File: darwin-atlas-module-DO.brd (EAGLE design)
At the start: 95 x 25 mm, 24 parts, among them J1 2X6-HEADERS, U3 M24C02-WMN6TP

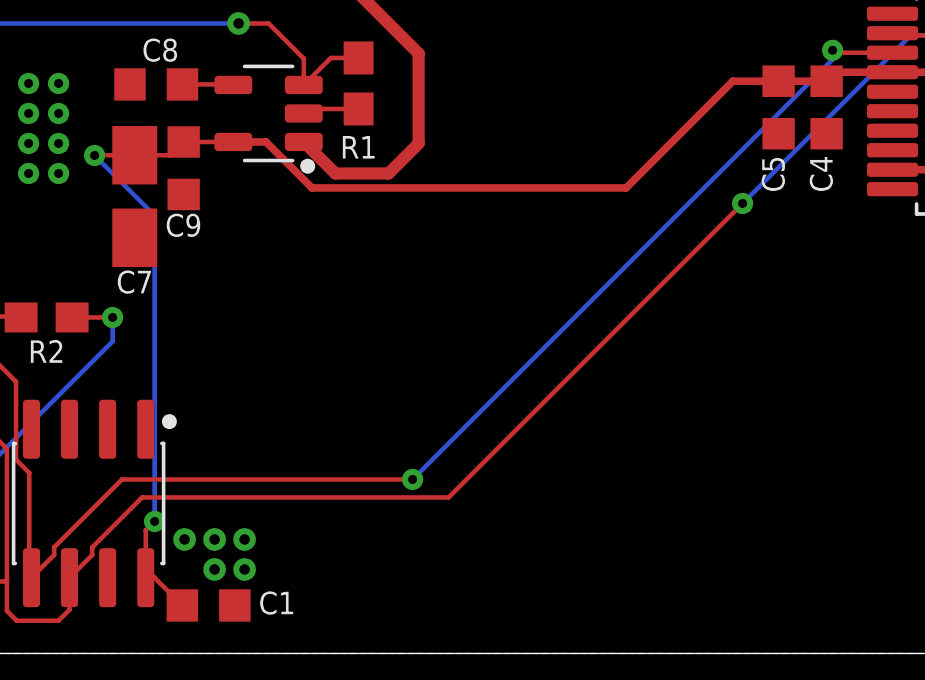
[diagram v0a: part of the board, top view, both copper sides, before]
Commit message: Forked D.O. Variant and added barometric pressure sensor to it.
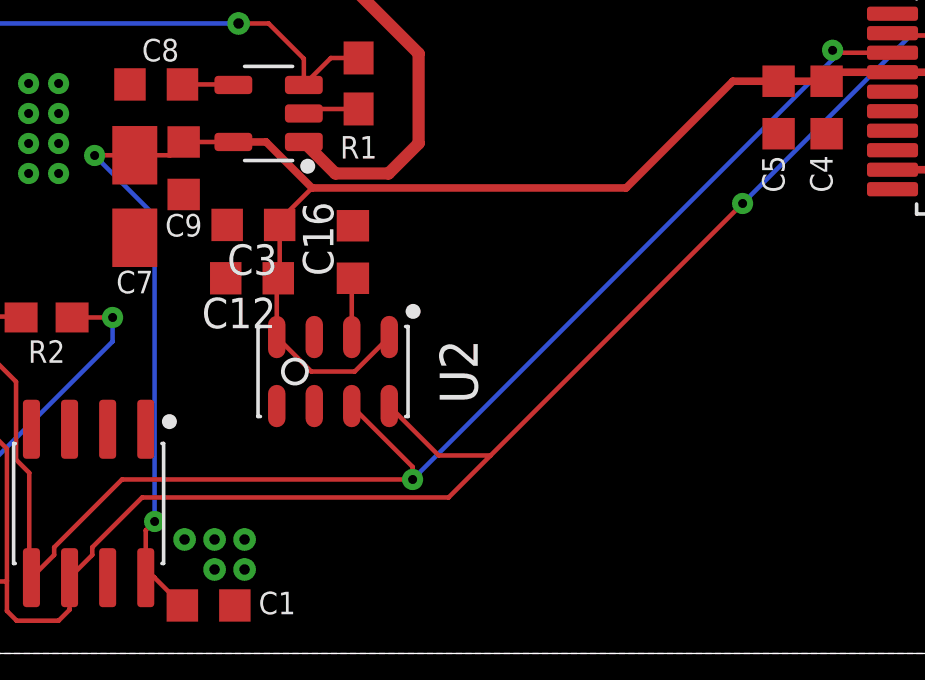
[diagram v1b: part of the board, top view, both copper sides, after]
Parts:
- added C12, C16: .1uf, rcl:C0603K
- added C3: 10uf, rcl:C0603K
- added U2: MPL3115A2LGA8, Conservify:SON125P300X500X110-8
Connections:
- new net CAP: C16.1, U2.2
- net 3V3: now also C12.1, C3.1, U2.1, U2.4
- net GND: now also C12.2, C16.2, C3.2, U2.3
- net SCL: now also U2.8
- net SDA: now also U2.7
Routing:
- net 3V3: track 51.8 -> 62.0 mm
- net SCL: track 51.6 -> 55.7 mm
- net SDA: track 48.5 -> 51.8 mm
- net CAP: track 0.00 -> 1.97 mm
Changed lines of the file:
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@@
 <attribute name="PROD_ID" value="RES-07828" x="55.6" y="20.4" size="1.778" layer="27" rot="R90" display="off"/>
+</element>
+<element name="U2" library="Conservify" library_urn="urn:adsk.eagle:library:11839183" package="SON125P300X500X110-8" package3d_urn="urn:adsk.eagle:package:11890235/2" value="MPL3115A2LGA8" x="23.147" y="9.398" smashed="yes" rot="R270">
+<attribute name="NAME" x="26.7019" y="9.398" size="1.27" layer="25" rot="R270" align="bottom-center"/>
+<attribute name="VALUE" x="20.012" y="9.398" size="1.27" layer="27" rot="R270" align="top-center"/>
+</element>
+<element name="C3" library="rcl" library_urn="urn:adsk.eagle:library:334" package="C0603K" package3d_urn="urn:adsk.eagle:package:23680/2" value="10uf" x="20.494" y="14.285" smashed="yes" rot="R180">
+<attribute name="NAME" x="21.294" y="13.635" size="1.016" layer="25" rot="R180"/>
+<attribute name="SPICEPREFIX" value="C" x="35.494" y="-0.715" size="1.778" layer="27" rot="R180" display="off"/>
+<attribute name="VALUE" x="21.294" y="15.935" size="1.016" layer="27" rot="R180"/>
+</element>
+<element name="C12" library="rcl" library_urn="urn:adsk.eagle:library:334" package="C0603K" package3d_urn="urn:adsk.eagle:package:23680/2" value=".1uf" x="20.447" y="12.507" smashed="yes" rot="R180">
+<attribute name="NAME" x="21.247" y="11.857" size="1.016" layer="25" rot="R180"/>
+<attribute name="SPICEPREFIX" value="C" x="40.447" y="2.507" size="1.778" layer="27" rot="R180" display="off"/>
+<attribute name="VALUE" x="21.247" y="14.157" size="1.016" layer="27" rot="R180"/>
+</element>
+<element name="C16" library="rcl" library_urn="urn:adsk.eagle:library:334" package="C0603K" package3d_urn="urn:adsk.eagle:package:23680/2" value=".1uf" x="23.81" y="13.382" smashed="yes" rot="R90">
+<attribute name="NAME" x="23.16" y="12.582" size="1.016" layer="25" rot="R90"/>
+<attribute name="SPICEPREFIX" value="C" x="18.81" y="-11.618" size="1.778" layer="27" rot="R90" display="off"/>
+<attribute name="VALUE" x="25.46" y="12.582" size="1.016" layer="27" rot="R90"/>
 </element>
 </elements>
@@
 <contactref element="C4" pad="2"/>
 <via x="13" y="16" extent="1-16" drill="0.3"/>
+<contactref element="U2" pad="3"/>
+<contactref element="C16" pad="2"/>
+<contactref element="C12" pad="2"/>
+<contactref element="C3" pad="2"/>
 </signal>
 <signal name="3V3">
@@
 <wire x1="15.2" y1="16.6" x2="15.207" y2="16.607" width="0.1524" layer="1"/>
 <wire x1="15.207" y1="16.607" x2="16.539" y2="16.607" width="0.1524" layer="1"/>
+<contactref element="U2" pad="1"/>
+<contactref element="C3" pad="1"/>
+<contactref element="C12" pad="1"/>
+<contactref element="U2" pad="4"/>
+<wire x1="21.272" y1="12.457" x2="21.272" y2="10.548" width="0.1524" layer="1"/>
+<wire x1="21.322" y1="12.507" x2="21.272" y2="12.457" width="0.1524" layer="1"/>
+<wire x1="21.369" y1="14.285" x2="21.369" y2="12.554" width="0.1524" layer="1"/>
+<wire x1="21.369" y1="12.554" x2="21.322" y2="12.507" width="0.1524" layer="1"/>
+<wire x1="21.369" y1="14.285" x2="21.369" y2="14.43805625" width="0.1524" layer="1"/>
+<wire x1="21.369" y1="14.43805625" x2="22.44834375" y2="15.5174" width="0.1524" layer="1"/>
+<wire x1="21.272" y1="10.548" x2="22.422" y2="9.398" width="0.1524" layer="1"/>
+<wire x1="23.872" y1="9.398" x2="25.022" y2="10.548" width="0.1524" layer="1"/>
+<wire x1="22.422" y1="9.398" x2="23.872" y2="9.398" width="0.1524" layer="1"/>
 </signal>
 <signal name="N$6">
@@
 <wire x1="13.02149375" y1="6.02149375" x2="13.02149375" y2="2.60010625" width="0.1524" layer="1"/>
 <wire x1="13.02149375" y1="2.60010625" x2="13.095" y2="2.5266" width="0.1524" layer="1"/>
+<contactref element="U2" pad="7"/>
+<wire x1="23.772" y1="8.248" x2="25.8" y2="6.22" width="0.1524" layer="1"/>
+<wire x1="25.8" y1="6.22" x2="25.8" y2="5.8" width="0.1524" layer="1"/>
 </signal>
 <signal name="SCL">
@@
 <wire x1="15.12185" y1="3.5388625" x2="16.7829875" y2="5.2" width="0.1524" layer="1"/>
 <wire x1="16.7829875" y1="5.2" x2="27" y2="5.2" width="0.1524" layer="1"/>
-<wire x1="27" y1="5.2" x2="36.8" y2="15" width="0.1524" layer="1"/>
+<wire x1="27" y1="5.2" x2="28.4" y2="6.6" width="0.1524" layer="1"/>
 <via x="36.8" y="15" extent="1-16" drill="0.3"/>
+<wire x1="28.4" y1="6.6" x2="36.8" y2="15" width="0.1524" layer="1"/>
 <wire x1="36.8" y1="15" x2="42.4" y2="20.6" width="0.1524" layer="16"/>
 <wire x1="42.4" y1="20.6" x2="43.8" y2="20.6" width="0.1524" layer="16"/>
@@
 <wire x1="43.8" y1="20.6" x2="41.8721" y2="20.6" width="0.1524" layer="1"/>
 <wire x1="41.8721" y1="20.6" x2="41.7971" y2="20.675" width="0.1524" layer="1"/>
+<contactref element="U2" pad="8"/>
+<wire x1="25.022" y1="8.248" x2="26.67" y2="6.6" width="0.1524" layer="1"/>
+<wire x1="26.67" y1="6.6" x2="28.4" y2="6.6" width="0.1524" layer="1"/>
 </signal>
 <signal name="WC">
@@
 <wire x1="53.85" y1="16.1" x2="53.6" y2="15.85" width="0.1524" layer="1"/>
 </signal>
+<signal name="CAP">
+<contactref element="U2" pad="2"/>
+<contactref element="C16" pad="1"/>
+<wire x1="23.772" y1="10.548" x2="23.772" y2="12.469" width="0.1524" layer="1"/>
+<wire x1="23.772" y1="12.469" x2="23.81" y2="12.507" width="0.1524" layer="1"/>
+</signal>
 </signals>
